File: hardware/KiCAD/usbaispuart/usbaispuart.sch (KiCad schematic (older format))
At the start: 51 parts, among them J1 AVR-ISP-UART-PROGRAMER-10, J2 LED Connector, J3 LED Connector, J4 USB_B, J5 Reset Jumper, J6 5V / 3.3 Selection Jumper, J7 Power Out Jumper, Q1 2N2222A, Q2 2N2222A, U1 SN74AHC367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

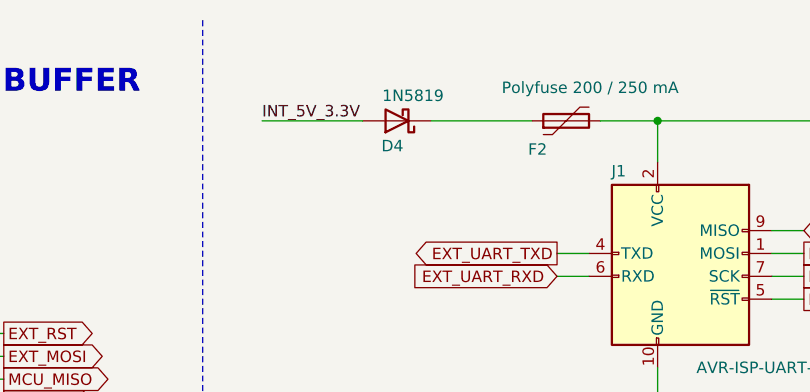
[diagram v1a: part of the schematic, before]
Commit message: Change D4 from 1N5819 to the correct 1N5817
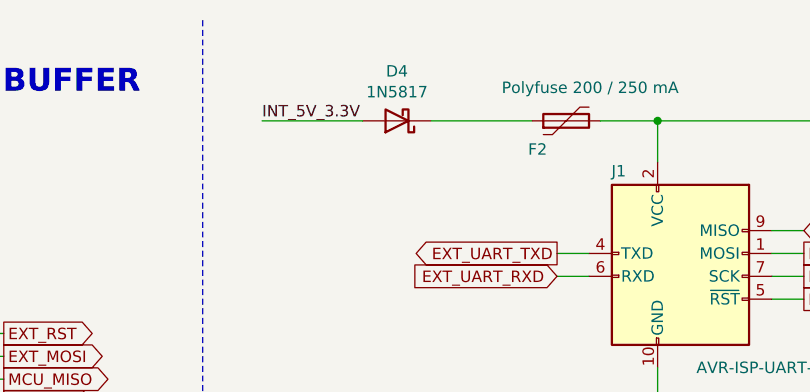
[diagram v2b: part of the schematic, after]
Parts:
- removed D4: 1N5819, Diode_THT:D_DO-41_SOD81_P2.54mm_Vertical_KathodeUp, symbol Diode:1N5819
- added D4: 1N5817, Diode_THT:D_DO-41_SOD81_P2.54mm_Vertical_KathodeUp, symbol Diode:1N5817
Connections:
- net INT_5V_3.3V: now also D4.2 (A)
- net at F2.1: now also D4.1 (K)
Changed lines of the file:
@@
 	0    -1   -1   0
-$EndComp
-$Comp
-L Diode:1N5819 D4
-U 1 1 6251013B
-P 7820 920
-F 0 "D4" H 7840 1030 50  0000 C CNN
-F 1 "1N5819" H 7750 810 50  0000 C CNN
-F 2 "Diode_THT:D_DO-41_SOD81_P2.54mm_Vertical_KathodeUp" H 7820 745 50  0001 C CNN
-F 3 "http://www.vishay.com/docs/88525/1n5817.pdf" H 7820 920 50  0001 C CNN
-	1    7820 920
-	-1   0    0    1
 $EndComp
 Wire Wire Line
@@
 Text Label 10810 920  2    50   ~ 0
 INT_EXT_5V_3.3V
+$Comp
+L Diode:1N5817 D4
+U 1 1 63B04224
+P 7820 920
+F 0 "D4" H 7820 703 50  0000 C CNN
+F 1 "1N5817" H 7820 794 50  0000 C CNN
+F 2 "Diode_THT:D_DO-41_SOD81_P2.54mm_Vertical_KathodeUp" H 7820 745 50  0001 C CNN
+F 3 "http://www.vishay.com/docs/88525/1n5817.pdf" H 7820 920 50  0001 C CNN
+	1    7820 920
+	-1   0    0    1
+$EndComp
 $EndSCHEMATC

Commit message: Bump version to 5a. + Fix an error trace. + Change C6 capacitor to electrolytic. + Rearrange layout to reduce noise.
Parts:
- removed C6: 2.2 μF / 16V, Capacitor_THT:C_Disc_D5.1mm_W3.2mm_P5.00mm, symbol Device:C
- added C6: 1 μF / 16V, Capacitor_THT:CP_Radial_D4.0mm_P2.00mm, symbol Device:CP
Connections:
- net GND: now also C6.2
- net VCC: now also C6.1
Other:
- note added: "Vout = 1.25 * ( 1 + RLow/RHigh)\n( consider voltage drop\n of PTC F2 and Diode D4 )\n\nRLow = R16\nJ6 Open: RHigh = R14\nJ6 Close: RHigh = R14, R15 in parallel"
- note removed: "Vout = 1.25 * ( 1 + R2/R1)\n( consider voltage drop\n of PTC F2 and Diode D4 )\n\nR2 = R16\nJ6 Open: R1 = R14\nJ6 Close: R1 = R14, R15 in parallel"
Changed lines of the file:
@@
 Sheet 1 1
 Title "USBaispUART ( CERN-OHL-S-2.0 licenced )"
-Date "2022-12-30"
-Rev "5"
+Date "2023-01-04"
+Rev "5a"
 Comp "www.nephelae.eu"
 Comment1 "USBaisp with UART"
@@
 F 3 "~" H 5410 6600 50  0001 C CNN
 	1    5410 6600
-	1    0    0    -1
-$EndComp
-$Comp
-L Device:C C6
-U 1 1 60EF15DE
-P 6365 6600
-F 0 "C6" H 6165 6600 50  0000 L CNN
-F 1 "2.2 μF / 16V" H 6395 6465 50  0000 L CNN
-F 2 "Capacitor_THT:C_Disc_D5.1mm_W3.2mm_P5.00mm" H 6403 6450 50  0001 C CNN
-F 3 "~" H 6365 6600 50  0001 C CNN
-	1    6365 6600
 	1    0    0    -1
 $EndComp
@@
 	8570 3430 8930 3430
 Text Notes 5230 4670 0    50   ~ 0
-Vout = 1.25 * ( 1 + R2/R1)\n( consider voltage drop\n  of PTC F2 and Diode D4 )\n\nR2 = R16\nJ6 Open: R1 = R14\nJ6 Close: R1 = R14, R15 in parallel
+Vout = 1.25 * ( 1 + RLow/RHigh)\n( consider voltage drop\n  of PTC F2 and Diode D4 )\n\nRLow = R16\nJ6 Open: RHigh = R14\nJ6 Close: RHigh = R14, R15 in parallel
 Text Notes 3880 4535 0    50   ~ 0
 Tantalum Low ESR
@@
 	-1   0    0    1
 $EndComp
+$Comp
+L Device:CP C6
+U 1 1 63B6D513
+P 6365 6600
+F 0 "C6" H 6483 6646 50  0000 L CNN
+F 1 "1 μF / 16V" H 6483 6555 50  0000 L CNN
+F 2 "Capacitor_THT:CP_Radial_D4.0mm_P2.00mm" H 6403 6450 50  0001 C CNN
+F 3 "~" H 6365 6600 50  0001 C CNN
+	1    6365 6600
+	1    0    0    -1
+$EndComp
 $EndSCHEMATC

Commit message: Update to 5b
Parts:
- added C10: 0.01 μF, Capacitor_THT:C_Disc_D4.7mm_W2.5mm_P5.00mm, symbol Device:C
- added C11: 10 μF / 25V, Capacitor_THT:CP_Radial_D4.0mm_P1.50mm, symbol Device:CP
- added H4: MountingHole, MountingHole:MountingHole_3.2mm_M3_DIN965, symbol Mechanical:MountingHole
- C6: value 1 μF / 16V -> 10 μF / 16V; footprint Capacitor_THT:CP_Radial_D4.0mm_P2.00mm -> Capacitor_THT:CP_Radial_D4.0mm_P1.50mm
- D4: footprint Diode_THT:D_DO-41_SOD81_P2.54mm_Vertical_KathodeUp -> Diode_THT:D_DO-41_SOD81_P5.08mm_Vertical_KathodeUp
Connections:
- net +6.5V: now also J7.2 (Pin_2); no longer U5.3 (VI)
- net GND: now also C10.2, C11.2
- net INT_5V_3.3V: now also C9.1, R14.1, R15.1, U5.2 (VO); no longer J7.1 (Pin_1)
- net VBUS: now also C11.1
- net at U2.21 (AREF): now also C10.1
- new net: J7.1 (Pin_1), U5.3 (VI)
- no-connect marks 9 -> 8
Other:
- note added: "Tantalum OR Low ESR"
- note removed: "Tantalum Low ESR"
- moved on the sheet: C13, C2, C3, C6, C7, C8, C9, D1, D2, D3, F1, J6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
